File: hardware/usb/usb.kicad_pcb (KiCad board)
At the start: 2 copper layers, 31.5 x 25.6 mm, 15 parts, among them J2 Conn_01x02, J3 Conn_01x02, J5 Conn_01x02, U1 USBLC6-2SC6, U2 AMS1117-3.3

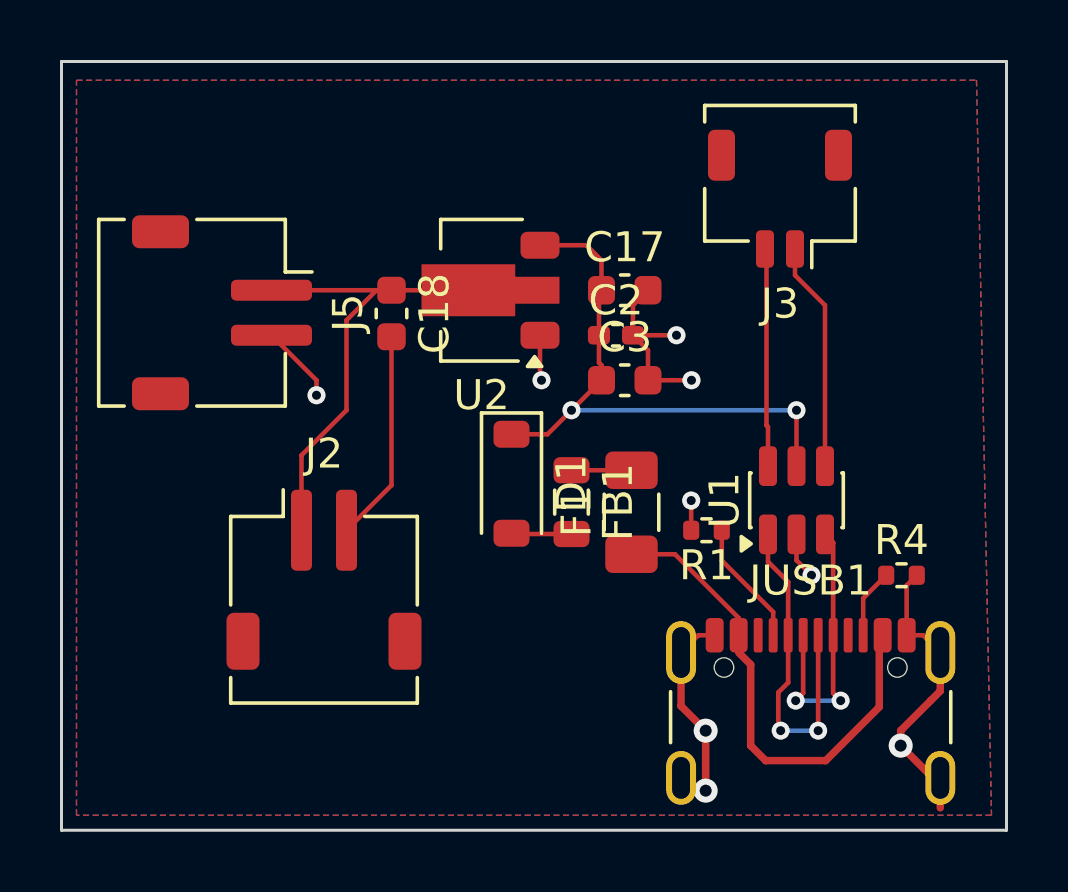
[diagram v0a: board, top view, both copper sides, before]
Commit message: simplify usb
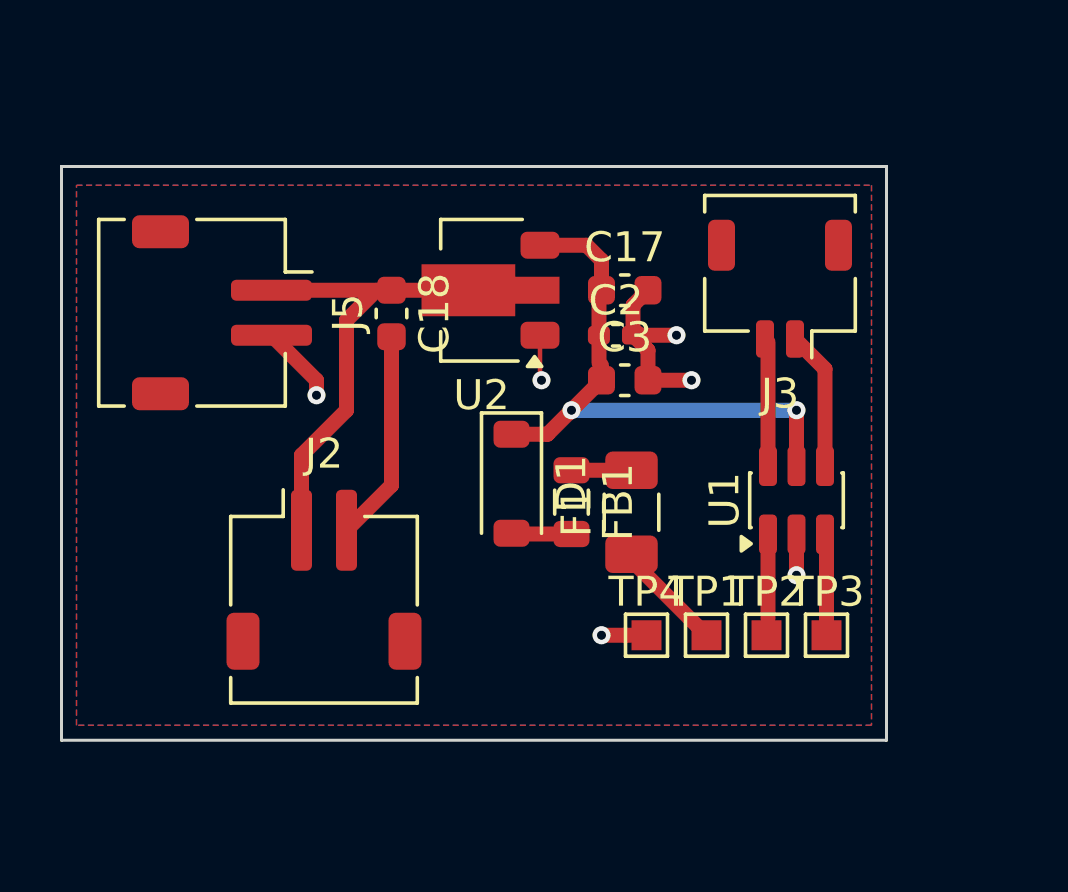
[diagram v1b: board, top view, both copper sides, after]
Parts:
- removed JUSB1: USB_C_Receptacle_USB2.0, Connector_USB:USB_C_Receptacle_GCT_USB4105-xx-A_16P_TopMnt_Horizontal
- removed R1, R4: 5.1K, Resistor_SMD:R_0402_1005Metric
- added TP1: TestPoint, TestPoint:TestPoint_Pad_1.0x1.0mm, F.Cu at (111.0, 80.5)
- added TP2: TestPoint, TestPoint:TestPoint_Pad_1.0x1.0mm, F.Cu at (113.0, 80.5)
- added TP3: TestPoint, TestPoint:TestPoint_Pad_1.0x1.0mm, F.Cu at (115.0, 80.5)
- added TP4: TestPoint, TestPoint:TestPoint_Pad_1.0x1.0mm, F.Cu at (109.0, 80.5)
- moved J3 3.00 mm to (113.5, 69.0)
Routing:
- net GND: track 34.4 -> 20.4 mm, vias 9 -> 6
- net Net-(F1-Pad1): track 16.0 -> 3.74 mm
- net /D-: track 11.4 -> 3.38 mm, vias 2 -> 0
- net /D+: track 9.54 -> 3.38 mm, vias 2 -> 0
- net /CC1: track 4.21 -> 0.00 mm
- net Net-(J3-Pin_1): track 7.65 -> 4.65 mm
- net Net-(J3-Pin_2): track 6.88 -> 4.28 mm
- net /CC2: track 2.32 -> 0.00 mm
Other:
- board size 31.5 x 25.6 mm -> 27.5 x 19.1 mm

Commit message: simplify pins and buttons
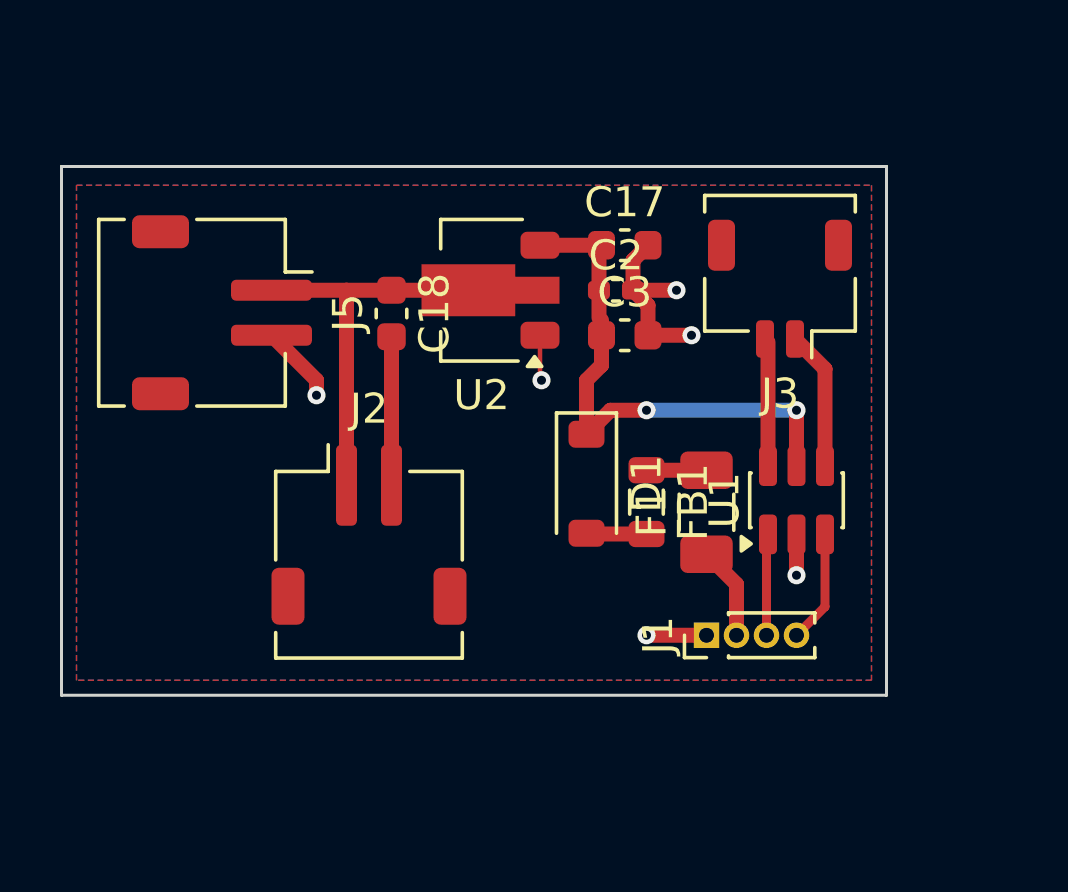
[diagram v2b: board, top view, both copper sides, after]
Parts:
- removed TP1, TP2, TP3, TP4: TestPoint, TestPoint:TestPoint_Pad_1.0x1.0mm
- added J1: Conn_01x04, Connector_PinHeader_1.00mm:PinHeader_1x04_P1.00mm_Vertical, F.Cu at (111.0, 80.5)
- moved D1 2.50 mm to (107.0, 75.5)
- moved F1 2.50 mm to (111.0, 76.4)
- moved FB1 2.50 mm to (109.0, 76.1)
- moved J2 2.12 mm to (99.8, 77.2)
- moved C17 1.50 mm to (108.3, 67.5)
- moved C2 1.50 mm to (108.0, 69.0)
- moved C3 1.50 mm to (108.3, 70.5)
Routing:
- net VCC: track 18.4 -> 15.4 mm
- net +5V: track 19.5 -> 17.8 mm
- net GND: track 20.4 -> 18.8 mm
- net Net-(J1-Pin_2): track 3.74 -> 3.11 mm
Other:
- board size 27.5 x 19.1 mm -> 27.5 x 17.6 mm

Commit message: adjustments
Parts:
- added TP1: TestPoint, TestPoint:TestPoint_Pad_1.0x1.0mm, F.Cu at (91.5, 76.0)
- added TP2: TestPoint, TestPoint:TestPoint_Pad_1.0x1.0mm, F.Cu at (91.5, 79.0)
- added TP3: TestPoint, TestPoint:TestPoint_Pad_1.0x1.0mm, F.Cu at (94.5, 76.0)
- added TP4: TestPoint, TestPoint:TestPoint_Pad_1.0x1.0mm, F.Cu at (94.5, 79.0)
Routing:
- net GND: track 18.8 -> 32.9 mm, vias 6 -> 7

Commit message: jlcpcb wip
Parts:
- removed TP1, TP2, TP3, TP4: TestPoint, TestPoint:TestPoint_Pad_1.0x1.0mm
- added J4: Conn_01x01, Connector_PinHeader_1.00mm:PinHeader_1x01_P1.00mm_Vertical, F.Cu at (91.5, 76.0)
- added J6: Conn_01x01, Connector_PinHeader_1.00mm:PinHeader_1x01_P1.00mm_Vertical, F.Cu at (94.5, 76.0)
- added J7: Conn_01x01, Connector_PinHeader_1.00mm:PinHeader_1x01_P1.00mm_Vertical, F.Cu at (91.5, 79.0)
- added J8: Conn_01x01, Connector_PinHeader_1.00mm:PinHeader_1x01_P1.00mm_Vertical, F.Cu at (94.5, 79.0)
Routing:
- net GND: track 32.9 -> 37.9 mm
- net VCC: track 15.4 -> 15.9 mm

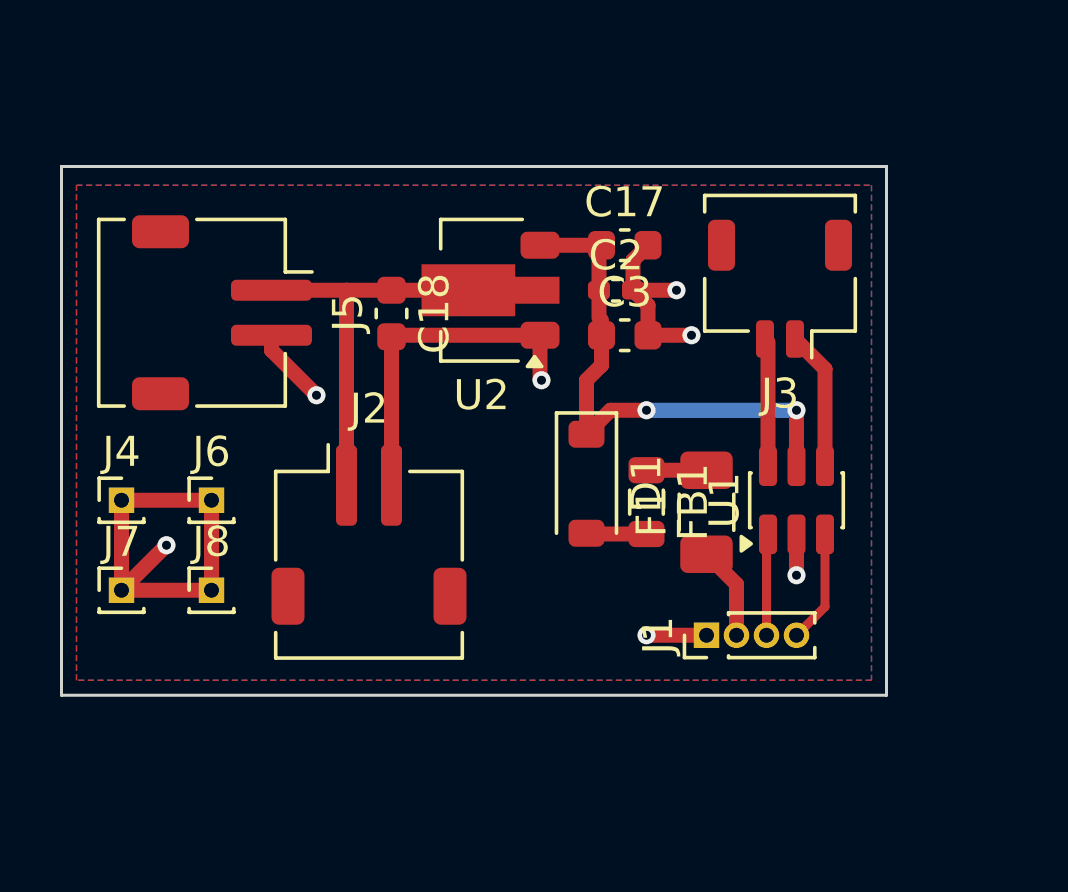
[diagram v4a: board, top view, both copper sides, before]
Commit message: replace connectors
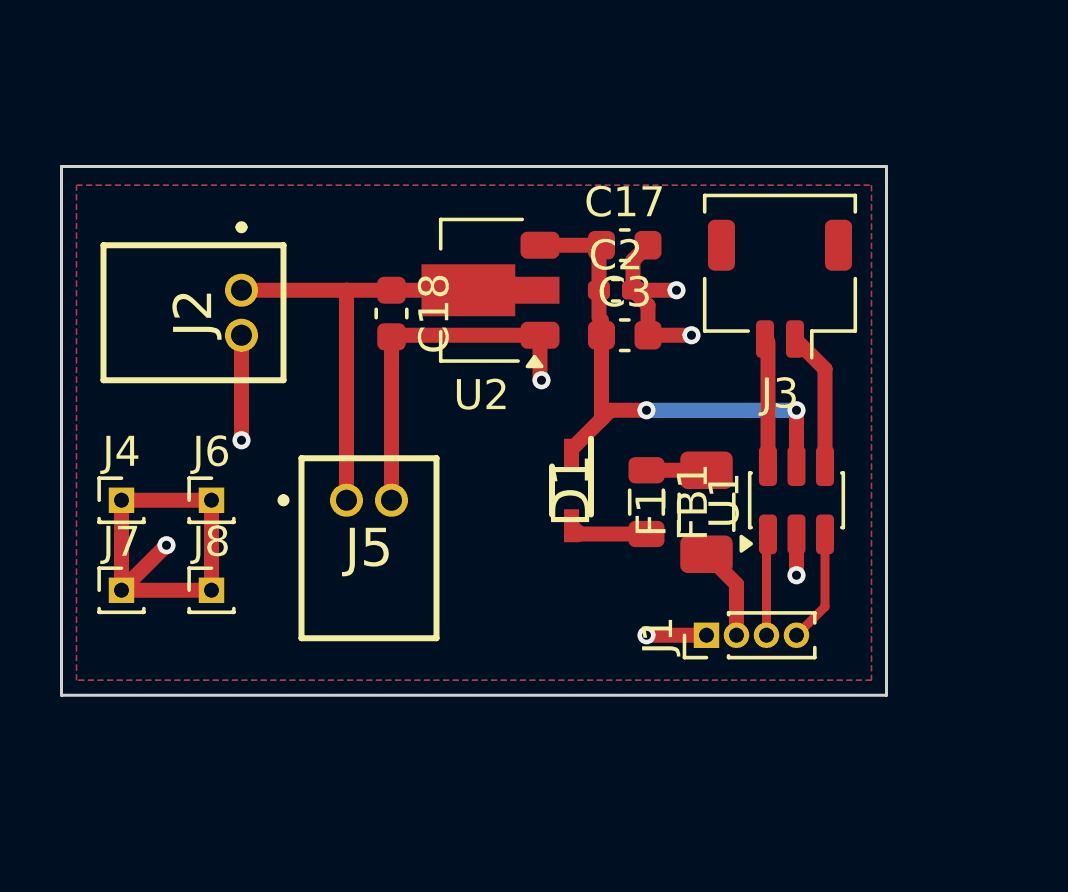
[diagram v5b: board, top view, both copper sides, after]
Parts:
- D1: footprint Diode_SMD:D_SOD-123 -> 1N5817WS:SOD2613X110N
- J2, J5: footprint Connector_JST:JST_ZH_S2B-ZR-SM4A-TF_1x02-1MP_P1.50mm_Horizontal -> LIB_S2B-ZR_LF__SN_:S2BZRLFSN
- moved J2 9.19 mm to (95.5, 69.0), turned to -90 degrees
- moved J5 7.50 mm to (99.0, 76.0), turned to 0 degrees
- moved D1 0.55 mm to (106.5, 75.7)
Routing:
- net VCC: track 15.9 -> 16.9 mm
- net GND: track 37.9 -> 38.7 mm
- net Net-(D1-A): track 2.01 -> 2.61 mm
